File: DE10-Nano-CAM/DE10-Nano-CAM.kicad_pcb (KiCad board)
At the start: 2 copper layers, 51.8 x 91.2 mm, 16 parts, among them J1 DF40C-100DS-0.4V_51_, J2 DF40C-100DS-0.4V_51_, J3 MEM2075-00-140-01-A, J4 Conn_02x20_Odd_Even, J5 52271-1579

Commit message: changed pcb
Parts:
- added R5: 4.7k, Resistor_SMD:R_0603_1608Metric, F.Cu at (152.3, 119.5)
- added R6: 4.7k, Resistor_SMD:R_0603_1608Metric, F.Cu at (155.4, 119.5)
- added R7: DNP, Resistor_SMD:R_0603_1608Metric, F.Cu at (147.1, 60.7)
- added R8: DNP, Resistor_SMD:R_0603_1608Metric, F.Cu at (148.7, 60.7)
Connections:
- J1 pad 15: unconnected-(J1-Pad15) -> /LVDS0_D0_N
- J1 pad 17: unconnected-(J1-Pad17) -> /LVDS0_D0_P
- J1 pad 21: unconnected-(J1-Pad21) -> /LVDS0_D1_N
- J1 pad 23: unconnected-(J1-Pad23) -> /LVDS0_D1_P
- J1 pad 27: unconnected-(J1-Pad27) -> /LVDS0_C_N
- J1 pad 29: unconnected-(J1-Pad29) -> /LVDS0_C_P
- J1 pad 33: unconnected-(J1-Pad33) -> /LVDS0_D2_N
- J1 pad 35: unconnected-(J1-Pad35) -> /LVDS0_D2_P
- J1 pad 39: unconnected-(J1-Pad39) -> /LVDS0_D3_N
- J1 pad 41: unconnected-(J1-Pad41) -> /LVDS0_D3_P
- J4 pad 17: /DATA_11 -> /LVDS0_D0_N
- J4 pad 19: unconnected-(J4-Pin_19-Pad19) -> /LVDS0_D0_P
- J4 pad 21: unconnected-(J4-Pin_21-Pad21) -> /DATA_11
- J4 pad 31: unconnected-(J4-Pin_31-Pad31) -> /SCL_DE10
- J4 pad 32: unconnected-(J4-Pin_32-Pad32) -> /SDA_DE10
- J4 pad 33: unconnected-(J4-Pin_33-Pad33) -> /LVDS0_D1_N
- J4 pad 34: unconnected-(J4-Pin_34-Pad34) -> /LVDS0_D2_N
- J4 pad 35: unconnected-(J4-Pin_35-Pad35) -> /LVDS0_D1_P
- J4 pad 36: unconnected-(J4-Pin_36-Pad36) -> /LVDS0_D2_P
- J4 pad 37: unconnected-(J4-Pin_37-Pad37) -> /LVDS0_C_N
- J4 pad 38: unconnected-(J4-Pin_38-Pad38) -> /LVDS0_D3_N
- J4 pad 39: unconnected-(J4-Pin_39-Pad39) -> /LVDS0_C_P
- J4 pad 40: unconnected-(J4-Pin_40-Pad40) -> /LVDS0_D3_P
- J5 pad 8: /DDMI0_CLK_N -> /LVDS1_C_N
- J5 pad 9: /DDMI0_CLK_P -> /LVDS1_C_P
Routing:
- added copper zone on In1.Cu, net +3V3
- added copper zone on In2.Cu, net +5V
- added copper zone on B.Cu, net GND
- added copper zone on F.Cu, net GND
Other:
- copper layers 2 -> 4

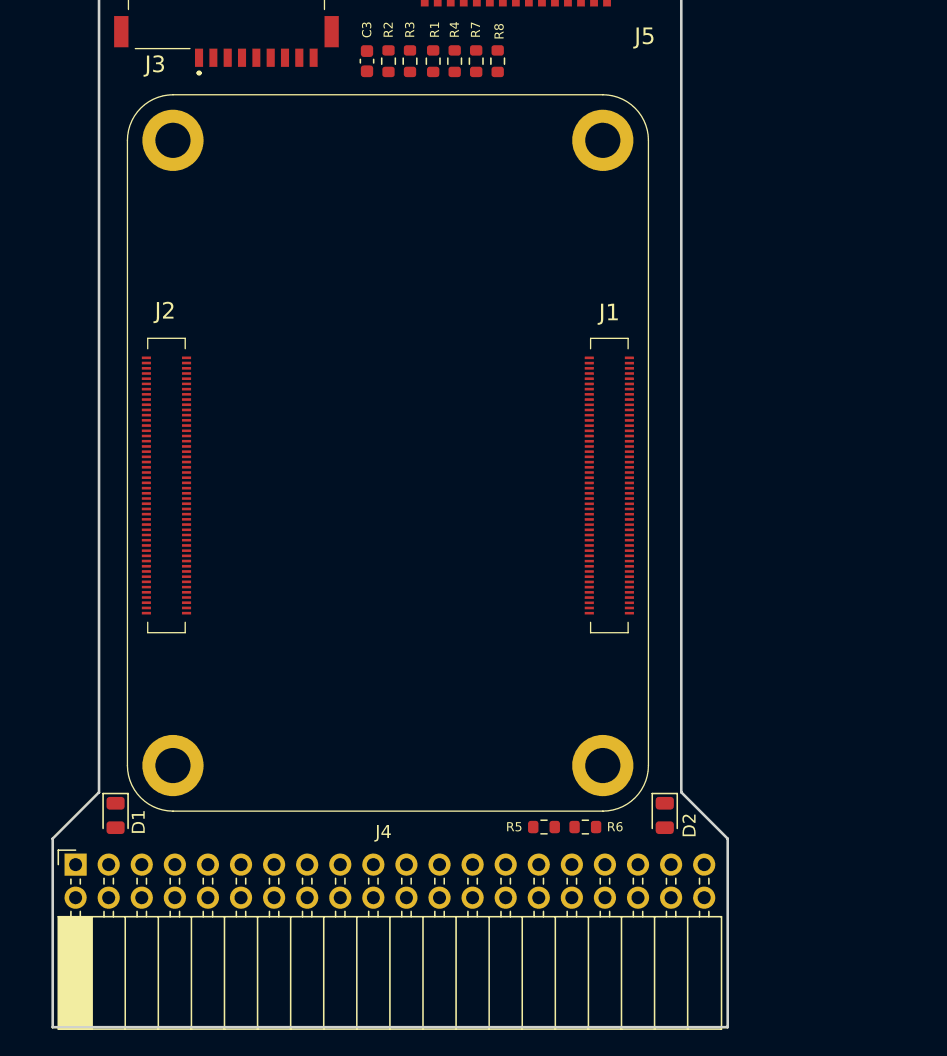
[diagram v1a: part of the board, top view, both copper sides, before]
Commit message: changes to DE10 schematic (GPIO)
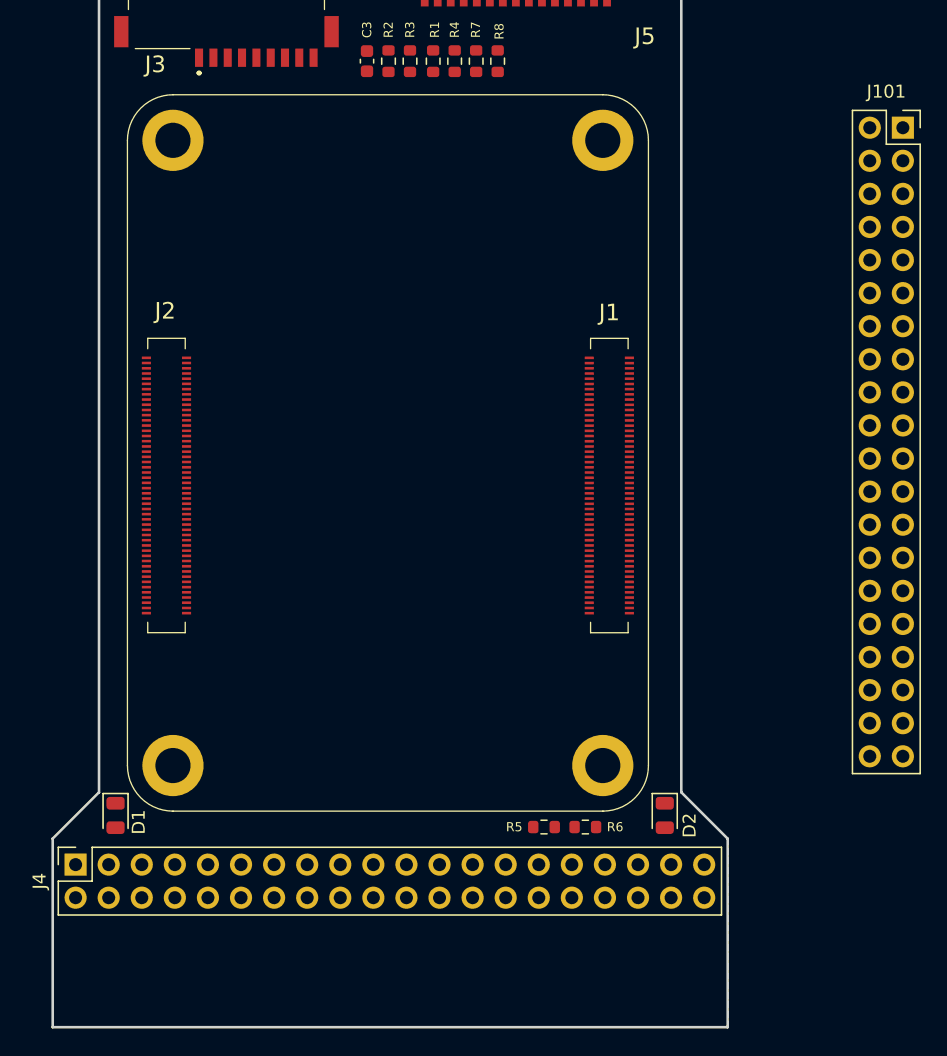
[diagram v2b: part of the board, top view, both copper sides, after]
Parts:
- added J101: Conn_02x20_Odd_Even, Connector_PinSocket_2.54mm:PinSocket_2x20_P2.54mm_Vertical, F.Cu at (179.8, 65.8)
- J4: footprint Connector_PinSocket_2.54mm:PinSocket_2x20_P2.54mm_Horizontal -> Connector_PinSocket_2.54mm:PinSocket_2x20_P2.54mm_Vertical
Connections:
- net Net-(J4-Pin_11) renamed +5V_DE10
- net Net-(J4-Pin_29) renamed +3.3V_DE10
- J1 pad 21: /LVDS0_D1_N -> unconnected-(J1-Pad21)
- J1 pad 23: /LVDS0_D1_P -> unconnected-(J1-Pad23)
- J1 pad 27: /LVDS0_C_N -> unconnected-(J1-Pad27)
- J1 pad 29: /LVDS0_C_P -> unconnected-(J1-Pad29)
- J1 pad 33: /LVDS0_D2_N -> unconnected-(J1-Pad33)
- J1 pad 35: /LVDS0_D2_P -> unconnected-(J1-Pad35)
- J1 pad 39: /LVDS0_D3_N -> unconnected-(J1-Pad39)
- J1 pad 41: /LVDS0_D3_P -> unconnected-(J1-Pad41)
- J1 pad 87: unconnected-(J1-Pad87) -> /LVDS1_C_N
- J1 pad 88: /DDMI0_CLK_P -> unconnected-(J1-Pad88)
- J1 pad 89: unconnected-(J1-Pad89) -> /LVDS1_C_P
- J1 pad 90: /DDMI0_CLK_N -> unconnected-(J1-Pad90)
- J2 pad 31: unconnected-(J2-Pad31) -> /DATA_14
- J2 pad 37: unconnected-(J2-Pad37) -> /DATA_15
- J2 pad 39: unconnected-(J2-Pad39) -> /DATA_16
- J2 pad 41: unconnected-(J2-Pad41) -> /DATA_17
- J2 pad 45: unconnected-(J2-Pad45) -> /DATA_18
- J2 pad 47: unconnected-(J2-Pad47) -> /DATA_19
- J2 pad 49: unconnected-(J2-Pad49) -> /DATA_20
- J4 pad 1: unconnected-(J4-Pin_1-Pad1) -> /DATA_14
- J4 pad 23: unconnected-(J4-Pin_23-Pad23) -> /DATA_16
- J4 pad 24: unconnected-(J4-Pin_24-Pad24) -> /DATA_21
- J4 pad 26: unconnected-(J4-Pin_26-Pad26) -> /DATA_22
- J4 pad 28: unconnected-(J4-Pin_28-Pad28) -> /DATA_23
- J4 pad 3: unconnected-(J4-Pin_3-Pad3) -> /DATA_15
- J4 pad 33: /LVDS0_D1_N -> /DATA_17
- J4 pad 34: /LVDS0_D2_N -> /DATA_24
- J4 pad 35: /LVDS0_D1_P -> /DATA_18
- J4 pad 36: /LVDS0_D2_P -> /DATA_25
- J4 pad 37: /LVDS0_C_N -> /DATA_19
- J4 pad 38: /LVDS0_D3_N -> /DATA_26
- J4 pad 39: /LVDS0_C_P -> /DATA_20
- J4 pad 40: /LVDS0_D3_P -> /DATA_27

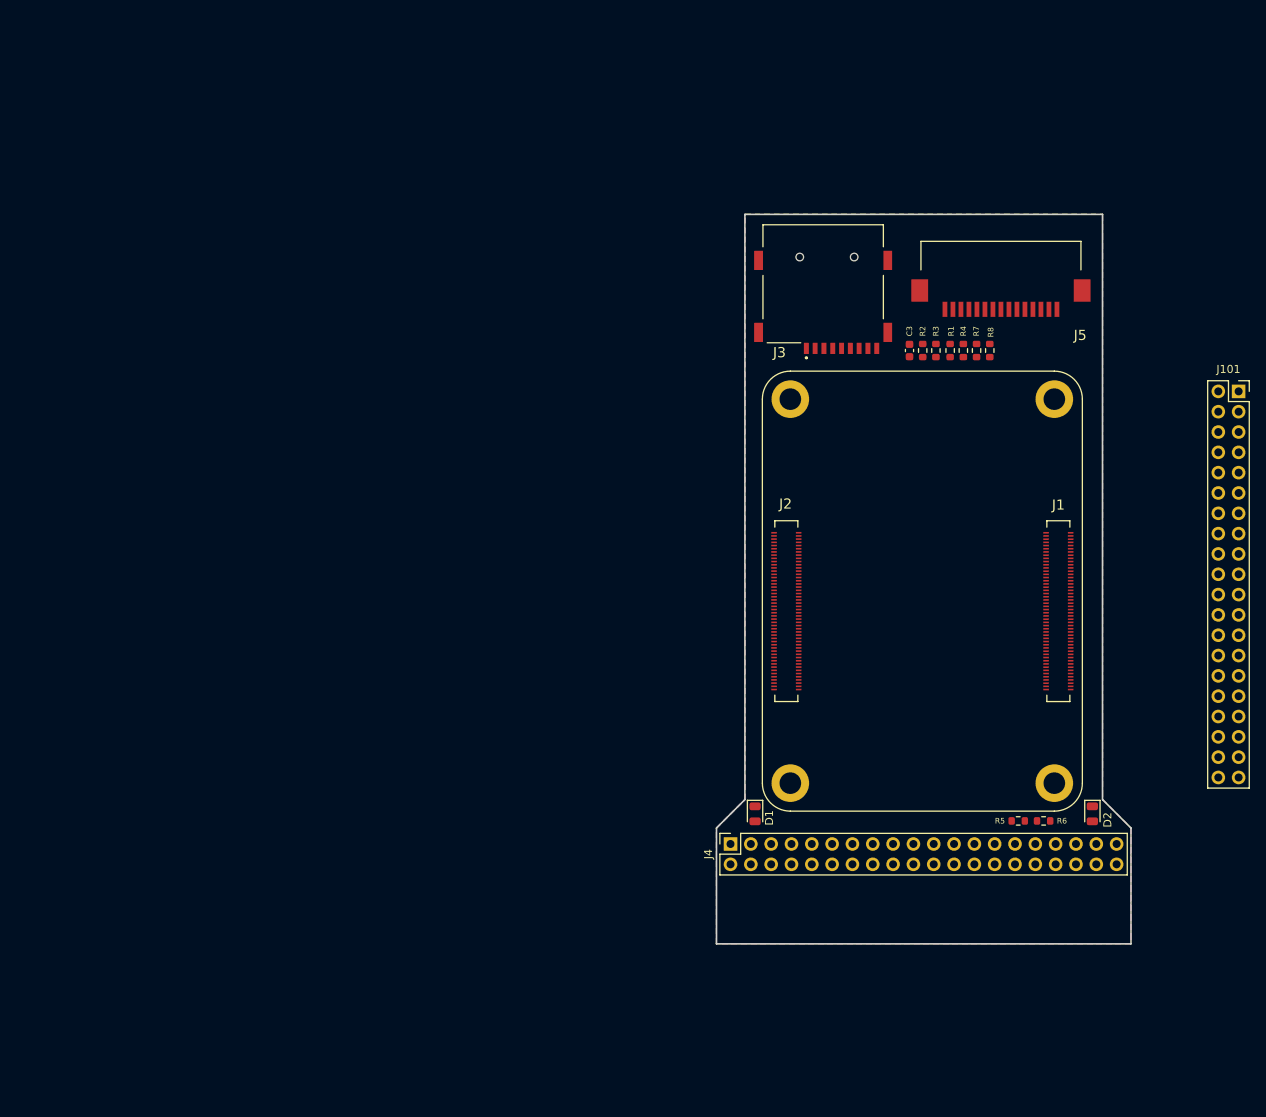
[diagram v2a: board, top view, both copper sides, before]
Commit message: changed PCB pinout
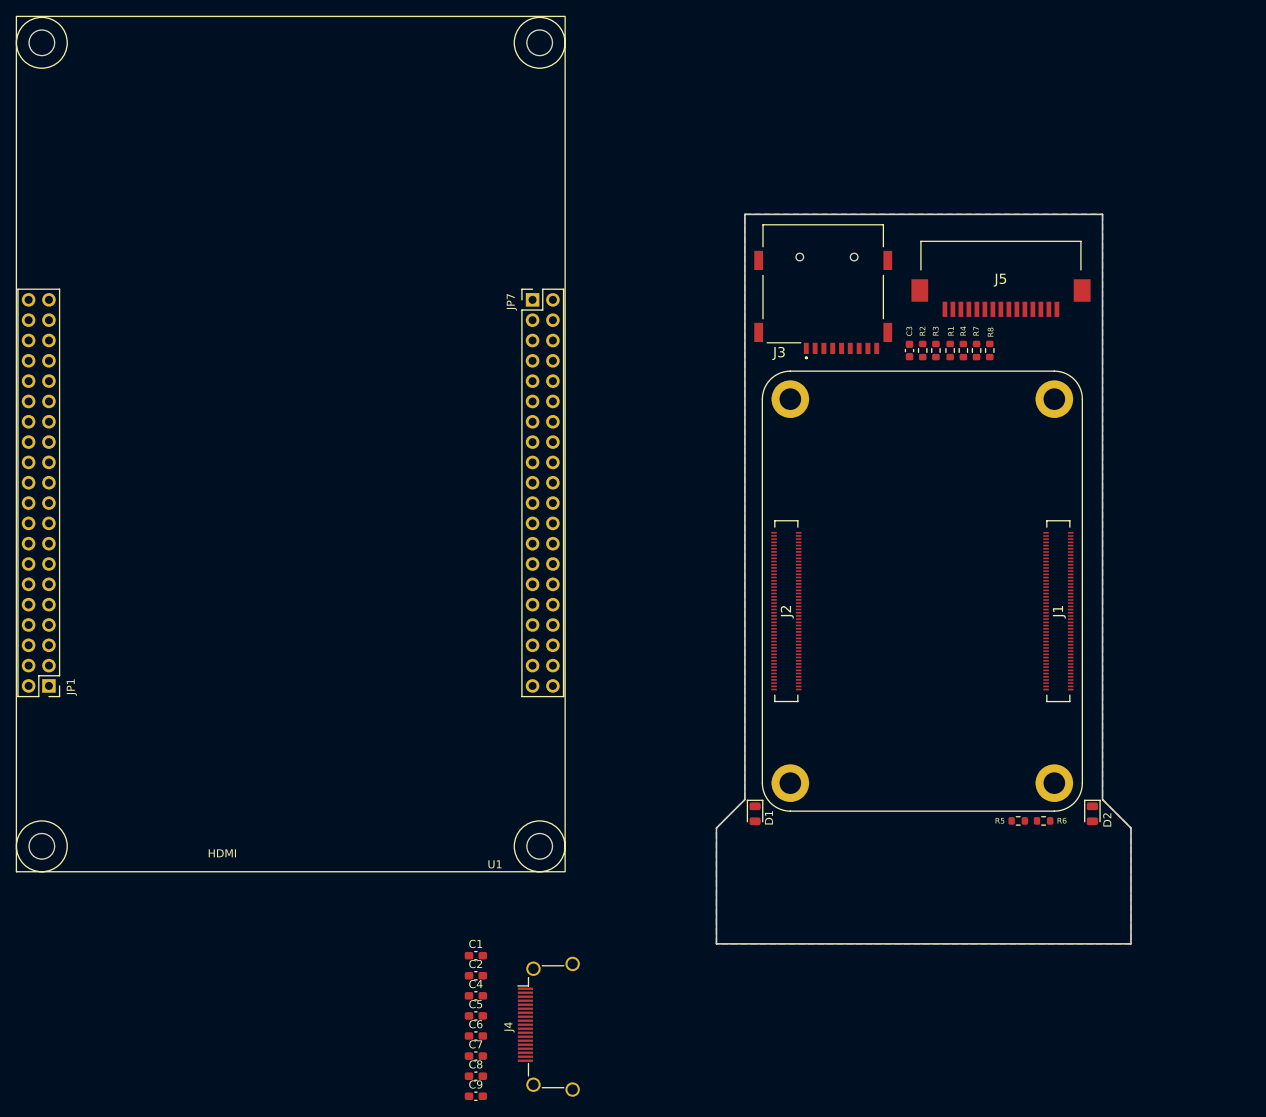
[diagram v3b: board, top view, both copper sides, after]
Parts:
- removed J101: Conn_02x20_Odd_Even, Connector_PinSocket_2.54mm:PinSocket_2x20_P2.54mm_Vertical
- added C1: 1µF, Capacitor_SMD:C_0603_1608Metric_Pad1.08x0.95mm_HandSolder, F.Cu at (84.5, 136.4)
- added C2: 1µF, Capacitor_SMD:C_0603_1608Metric_Pad1.08x0.95mm_HandSolder, F.Cu at (84.5, 138.9)
- added C4: 1µF, Capacitor_SMD:C_0603_1608Metric_Pad1.08x0.95mm_HandSolder, F.Cu at (84.5, 141.4)
- added C5: 1µF, Capacitor_SMD:C_0603_1608Metric_Pad1.08x0.95mm_HandSolder, F.Cu at (84.5, 143.9)
- added C6: 1µF, Capacitor_SMD:C_0603_1608Metric_Pad1.08x0.95mm_HandSolder, F.Cu at (84.5, 146.4)
- added C7: 1µF, Capacitor_SMD:C_0603_1608Metric_Pad1.08x0.95mm_HandSolder, F.Cu at (84.5, 148.9)
- added C8: 1µF, Capacitor_SMD:C_0603_1608Metric_Pad1.08x0.95mm_HandSolder, F.Cu at (84.5, 151.4)
- added C9: 1µF, Capacitor_SMD:C_0603_1608Metric_Pad1.08x0.95mm_HandSolder, F.Cu at (84.5, 153.9)
- added U1: ~, Lib:DE10-Nano, F.Cu at (92.5, 122.7)
- J4: value Conn_02x20_Odd_Even -> HDMI_A; footprint Connector_PinSocket_2.54mm:PinSocket_2x20_P2.54mm_Vertical -> Connector_Video:HDMI_A_Amphenol_10029449-x01xLF_Horizontal
- moved J4 30.8 mm to (95.7, 145.2)
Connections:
- D1 pad 2: +5V_DE10 -> /+5V_DE10
- D2 pad 2: +3.3V_DE10 -> /+3.3V_DE10
- J1 pad 21: unconnected-(J1-Pad21) -> /LVDS0_D1_N
- J1 pad 23: unconnected-(J1-Pad23) -> /LVDS0_D1_P
- J1 pad 27: unconnected-(J1-Pad27) -> /LVDS0_C_N
- J1 pad 29: unconnected-(J1-Pad29) -> /LVDS0_C_P
- J1 pad 33: unconnected-(J1-Pad33) -> /CAM_SDA0
- J1 pad 35: unconnected-(J1-Pad35) -> /CAM_SCL0
- J1 pad 39: unconnected-(J1-Pad39) -> /ENABLE
- J1 pad 41: unconnected-(J1-Pad41) -> /PIXEL_CLK
- J1 pad 70: unconnected-(J1-Pad70) -> /GPIO_EB_5_P
- J1 pad 72: unconnected-(J1-Pad72) -> /GPIO_EB_5_N
- J1 pad 75: /LVDS1_D0_N -> /DATA_22
- J1 pad 76: unconnected-(J1-Pad76) -> /GPIO_EB_4_P
- J1 pad 77: /LVDS1_D0_P -> /DATA_23
- J1 pad 78: unconnected-(J1-Pad78) -> /GPIO_EB_4_N
- J1 pad 81: /LVDS1_D1_N -> /DATA_24
- J1 pad 82: unconnected-(J1-Pad82) -> /GPIO_EB_2_P
- J1 pad 83: /LVDS1_D1_P -> /DATA_25
- J1 pad 84: unconnected-(J1-Pad84) -> /GPIO_EB_2_N
- J1 pad 87: /LVDS1_C_N -> /DATA_26
- J1 pad 88: unconnected-(J1-Pad88) -> /GPIO_EB_0_P
- J1 pad 89: /LVDS1_C_P -> /DATA_27
- J1 pad 90: unconnected-(J1-Pad90) -> /GPIO_EB_0_N
- J1 pad 93: unconnected-(J1-Pad93) -> /DATA_28
- J1 pad 95: unconnected-(J1-Pad95) -> /DATA_29
- J2 pad 25: /DATA_11 -> /DATA_30
- J2 pad 27: /DATA_12 -> /DATA_31
- J2 pad 29: /DATA_13 -> /DATA_32
- J2 pad 31: /DATA_14 -> /DATA_33
- J2 pad 37: /DATA_15 -> /DATA_14
- J2 pad 39: /DATA_16 -> /DATA_15
- J2 pad 41: /DATA_17 -> /DATA_16
- J2 pad 45: /DATA_18 -> /DATA_17
- J2 pad 47: /DATA_19 -> /DATA_18
- J2 pad 49: /DATA_20 -> /DATA_19
- J2 pad 51: /VSYNC -> /DATA_20
- J2 pad 54: /PIXEL_CLK -> /DATA_11
- J2 pad 55: /ENABLE -> GND
- J2 pad 56: unconnected-(J2-Pad56) -> /DATA_12
- J2 pad 58: /HSYNC -> /DATA_13
- J2 pad 80: /SCL0 -> /DE10_SCL0
- J2 pad 82: /SDA0 -> /DE10_SDA0
- J4 pad 1: /DATA_14 -> /D2+
- J4 pad 10: /DATA_6 -> /CK+
- J4 pad 11: +5V_DE10 -> GND
- J4 pad 12: GND -> /CK-
- J4 pad 13: /DATA_7 -> unconnected-(J4-CEC-Pad13)
- J4 pad 14: /DATA_8 -> unconnected-(J4-UTILITY-Pad14)
- J4 pad 15: /DATA_9 -> unconnected-(J4-SCL-Pad15)
- J4 pad 16: /DATA_10 -> unconnected-(J4-SDA-Pad16)
- J4 pad 17: /LVDS0_D0_N -> GND
- J4 pad 18: /DATA_12 -> +5V
- J4 pad 19: /LVDS0_D0_P -> unconnected-(J4-HPD-Pad19)
- J4 pad 2: /PIXEL_CLK -> GND
- J4 pad 3: /DATA_15 -> /D2-
- J4 pad 4: /DATA_0 -> /D1+
- J4 pad 5: /DATA_1 -> GND
- J4 pad 6: /DATA_2 -> /D1-
- J4 pad 7: /DATA_3 -> /D0+
- J4 pad 8: /DATA_4 -> GND
- J4 pad 9: /DATA_5 -> /D0-
- J5 pad 13: /SCL0 -> /CAM_SCL0
- J5 pad 14: /SDA0 -> /CAM_SDA0
- J5 pad 2: /LVDS1_D0_N -> /LVDS0_D0_N
- J5 pad 3: /LVDS1_D0_P -> /LVDS0_D0_P
- J5 pad 5: /LVDS1_D1_N -> /LVDS0_D1_N
- J5 pad 6: /LVDS1_D1_P -> /LVDS0_D1_P
- J5 pad 8: /LVDS1_C_N -> /LVDS0_C_N
- J5 pad 9: /LVDS1_C_P -> /LVDS0_C_P
- R5 pad 1: /SCL_DE10 -> /DE10_SCL0
- R6 pad 1: /SDA_DE10 -> /DE10_SDA0
- R7 pad 1: /SCL0 -> /CAM_SCL0
- R8 pad 1: /SDA0 -> /CAM_SDA0
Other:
- board size 51.8 x 91.2 mm -> 65.4 x 103.6 mm

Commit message: changed minor pin fixes
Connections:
- J1 pad 94: unconnected-(J1-Pad94) -> /HSYNC
- J1 pad 96: unconnected-(J1-Pad96) -> /VSYNC
- U1 pad 1_17: /LVDS0_D0_N -> /DATA_14
- U1 pad 1_19: /LVDS0_D0_P -> /DATA_15
- U1 pad 1_21: /DATA_14 -> /DATA_16
- U1 pad 1_22: /DATA_15 -> /DATA_17
- U1 pad 1_23: /DATA_16 -> /DATA_18
- U1 pad 1_24: /DATA_17 -> /DATA_19
- U1 pad 1_26: /DATA_18 -> /DATA_20
- U1 pad 1_28: /DATA_19 -> GND
- U1 pad 1_33: /DATA_20 -> /DATA_22
- U1 pad 1_34: GND -> /DATA_23
- U1 pad 1_35: /DATA_22 -> /DATA_24
- U1 pad 1_36: /DATA_23 -> /DATA_25
- U1 pad 1_37: /DATA_24 -> /DATA_26
- U1 pad 1_38: /DATA_25 -> /DATA_27
- U1 pad 1_39: /DATA_26 -> /DATA_28
- U1 pad 1_40: /DATA_27 -> unconnected-(U1-Pad1_40)
- U1 pad 7_1: /DATA_28 -> /ENABLE
- U1 pad 7_2: unconnected-(U1-Pad7_2) -> /DATA_30
- U1 pad 7_3: /ENABLE -> /DATA_31
- U1 pad 7_4: /DATA_30 -> /DATA_32
- U1 pad 7_5: /DATA_31 -> /DATA_33
- U1 pad 7_6: /DATA_32 -> unconnected-(U1-Pad7_6)
- U1 pad 7_7: /DATA_33 -> unconnected-(U1-Pad7_7)
